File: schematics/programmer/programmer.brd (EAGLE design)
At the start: 40 x 25 mm, 16 parts, among them CN1 M05X2-0.05-SMD, IC1 CY7C68013A-56PVXC, U2 TLV702XX, Y1 24MHz

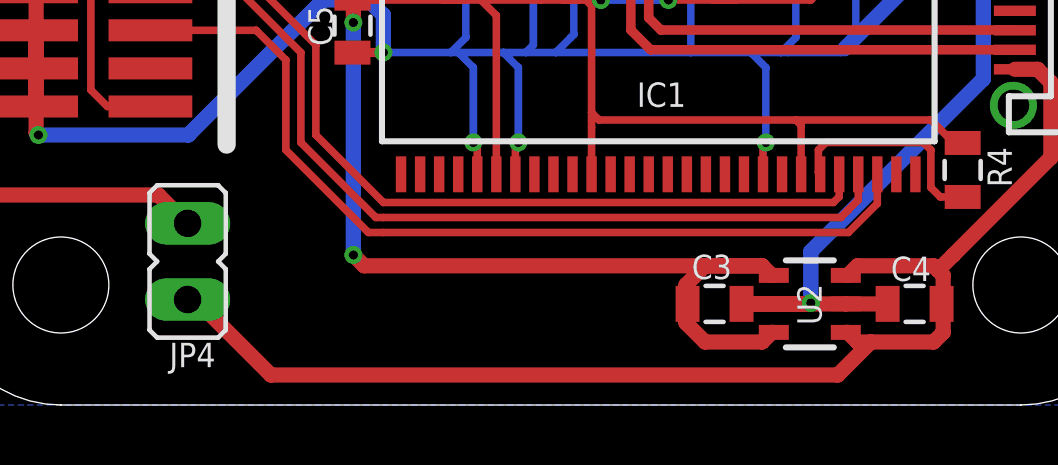
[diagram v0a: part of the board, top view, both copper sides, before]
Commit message: Fixed both Loki and the programmer to use 3.3v for power on programming headers.
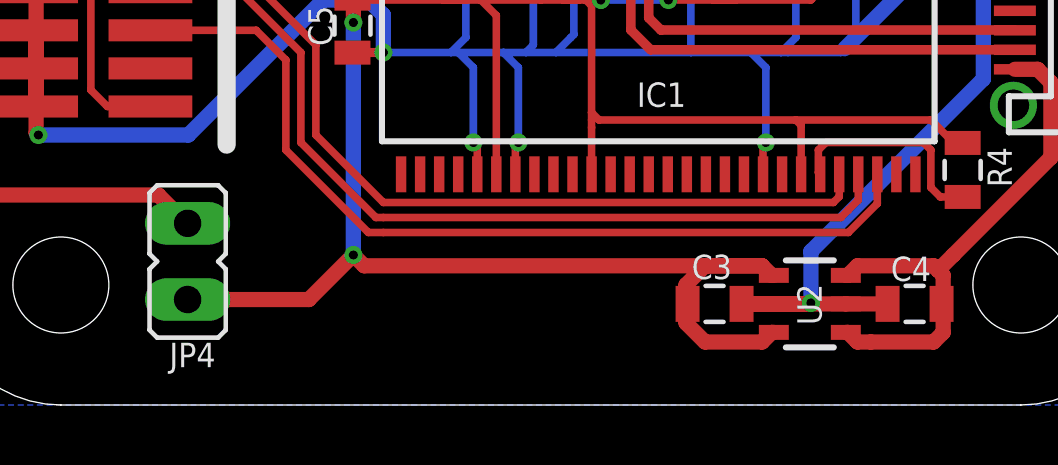
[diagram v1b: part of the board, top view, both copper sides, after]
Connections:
- net VBUS: no longer JP4.1
- net VCC: now also JP4.1
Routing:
- net VBUS: track 42.4 -> 18.2 mm
- net VCC: track 107.6 -> 113.7 mm
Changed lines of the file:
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@@
 <wire x1="28.675" y1="7.69" x2="28.675" y2="9.325" width="0.254" layer="1"/>
 <wire x1="28.675" y1="9.325" x2="28.5" y2="9.5" width="0.254" layer="1"/>
+<contactref element="JP4" pad="1"/>
+<wire x1="8.225" y1="3.515" x2="12.265" y2="3.515" width="0.508" layer="1"/>
+<wire x1="12.265" y1="3.515" x2="13.75" y2="5" width="0.508" layer="1"/>
 </signal>
 <signal name="/RST">
@@
 <contactref element="U2" pad="3"/>
 <contactref element="U$3" pad="VBUS"/>
-<contactref element="JP4" pad="1"/>
 <wire x1="30.165" y1="2.42" x2="30.2325" y2="2.42" width="0.508" layer="1"/>
 <wire x1="30.2325" y1="2.42" x2="30.5525" y2="2.1" width="0.508" layer="1"/>
@@
 <wire x1="37" y1="8.25" x2="33.75" y2="5" width="0.508" layer="1"/>
 <wire x1="33.24125" y1="4.49125" x2="33.75" y2="5" width="0.508" layer="1"/>
-<wire x1="8.225" y1="3.515" x2="8.485" y2="3.515" width="0.508" layer="1"/>
-<wire x1="8.485" y1="3.515" x2="11" y2="1" width="0.508" layer="1"/>
-<wire x1="11" y1="1" x2="29.9" y2="1" width="0.508" layer="1"/>
-<wire x1="29.9" y1="1" x2="31" y2="2.1" width="0.508" layer="1"/>
+<wire x1="8.485" y1="3.515" x2="11" y2="1" width="0" layer="19" extent="1-16"/>
+<wire x1="11" y1="1" x2="29.9" y2="1" width="0" layer="19" extent="1-16"/>
+<wire x1="29.9" y1="1" x2="31" y2="2.1" width="0" layer="19" extent="1-16"/>
 </signal>
 <signal name="N$3">
